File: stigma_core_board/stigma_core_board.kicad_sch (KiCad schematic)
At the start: 83 parts, among them J1 TC2050, J5 USB_C_Receptacle_USB2.0, SW1 KMR721NGLFS, SW2 KMR721NGLFS, U1 STM32H743VITx, U10 H3LIS331DL, U11 MS5607/MS5611, U12 LIS3MDL, U13 BMP580/BMP388/LPS22, U2 TPD4E1U06, U3 BMP580/BMP388/LPS22, U4 IIM-42652 (or other LGA-14 IM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, U5 AZ1117I-3.3, U6 ICM-42688 (or other LGA-14 IM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, U8 W25Q128JVP, U9 LSM6DSR, Y1 25MHz, Y2 32.768kHz

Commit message: First pass of signal routing
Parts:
- added C39, C40: 100n, Capacitor_SMD:C_0402_1005Metric, symbol Device:C_Small
- added R14: 4k7, Resistor_SMD:R_0402_1005Metric, symbol Device:R_Small
- added R15: 10k, Resistor_SMD:R_0402_1005Metric, symbol Device:R_Small
- added R16, R17, R18, R19, R20: 22, Resistor_SMD:R_0402_1005Metric, symbol Device:R_Small
- added U7: TPD4E1U06, Package_TO_SOT_SMD:SOT-563, symbol stigma:TPD4E001DRL
- J3: footprint stigma:DF40GB-70DP-0.4V -> stigma:DF40GB-70DP-0.4V-plug; symbol Connector_Generic:Conn_02x35_Top_Bottom -> Connector_Generic_Shielded:Conn_02x35_Top_Bottom_Shielded
- U2: footprint Package_TO_SOT_SMD:SOT-23-6 -> Package_TO_SOT_SMD:SOT-563; symbol Power_Protection:SRV05-4 -> stigma:TPD4E001DRL
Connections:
- net +3.3V: now also U7.5 (IO4)
- net +5V: now also C39.2, U7.6 (V_{cc})
- net BOOT: now also U2.2 (IO2), R20.1
- net D0+: now also U2.4 (IO3); no longer U2.6 (IO4)
- net D0-: now also U2.5 (IO4); no longer U2.4 (IO3)
- net GND: now also J3.SH (Shield), U2.3 (GND), C39.1, C40.1, R15.1, U7.3 (GND); no longer U2.2 (VN)
- net LED_GREEN: now also U1.77 (PA15)
- net LED_RED: now also U1.67 (PA8)
- net LED_YELLOW: now also U1.69 (PA10)
- net NRST: now also U2.1 (IO1), R17.1; no longer U1.14 (NRST)
- net SPI1_CS_BARO1: now also U1.83 (PD2)
- net SPI1_CS_HIGHG: now also U1.56 (PD9)
- net SPI1_CS_IMU1: now also U1.85 (PD4)
- net SPI1_CS_MAG: now also U1.86 (PD5)
- net SPI2_CS_BARO2: now also U1.3 (PE4)
- net SPI2_CS_BARO3: now also U1.2 (PE3)
- net SPI2_CS_IMU2: now also U1.55 (PD8)
- net SPI2_CS_IMU3: now also U1.7 (PC13)
- net SPI3_CS_FLASH: now also U1.87 (PD6); no longer U1.7 (PC13)
- net SWCLK: now also R16.2; no longer J1.6 (Pin_6)
- net SWDIO: now also R18.1; no longer J1.2 (Pin_2)
- net SWO: now also R19.1; no longer J1.5 (Pin_5)
- net USB_FS_VBUS: now also R14.1, R15.2
- net at D4.2 (A), J5.A4 (VBUS), J5.A9 (VBUS)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: now also U2.6 (V_{cc}), C40.2, R14.2; no longer U2.5 (VP)
- net BOOT0: no longer names the net of U1.94 (BOOT0)
- net BOOT0: now also R20.2
- net PA1 renamed PA1_ETH_REF_CLK
- net PA2 renamed PA2_ETH_MDIO
- net PA7 renamed PA7_ETH_CRS_DV
- net PB11 renamed PB11_ETH_TX_EN
- net PB12 renamed ETH_TXD-
- net PB13 renamed ETH_TXD+
- net PC1 renamed PC1_ETH_MDC
- net PC4 renamed ETH_RXD-
- net PC5 renamed ETH_RXD+
- new net: R17.2, U1.14 (NRST)
- new net: J1.5 (Pin_5), R19.2, U7.1 (IO1)
- new net: J1.2 (Pin_2), R18.2, U7.2 (IO2)
- new net: J1.6 (Pin_6), R16.1, U7.4 (IO3)
- no-connect marks 14 -> 18
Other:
- note added: "TODO: load cap values"
- note removed: "TODO: VBUS detection"
- note removed: "TODO: clamping diodes for buttons?"
- note removed: "TODO: place voltage dividers for battery voltage/current sensing here?"
- moved on the sheet: C15, C18, C19, C20, J1, R5, R6, SW1, SW2, U2, U5, U8

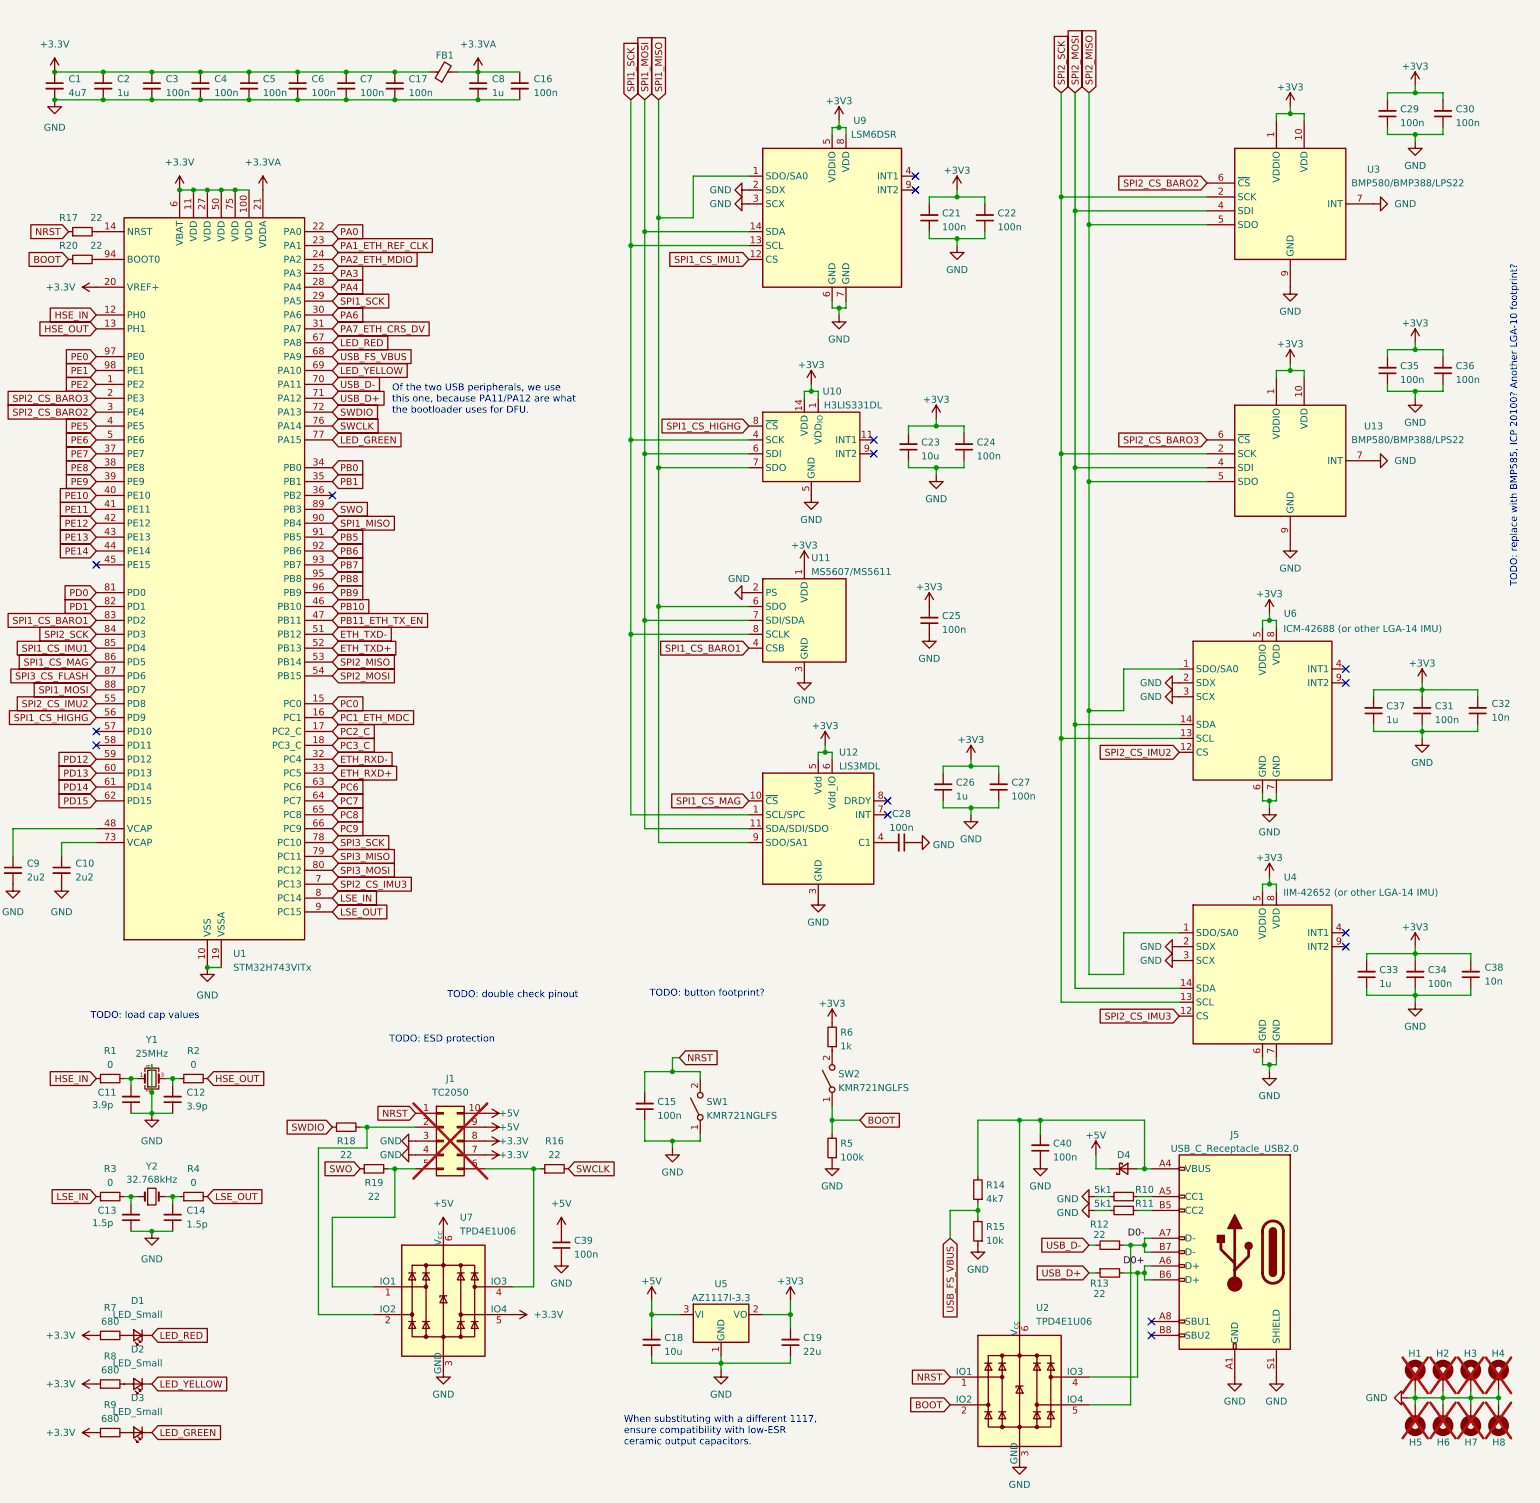
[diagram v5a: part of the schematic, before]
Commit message: Route power, please DRC
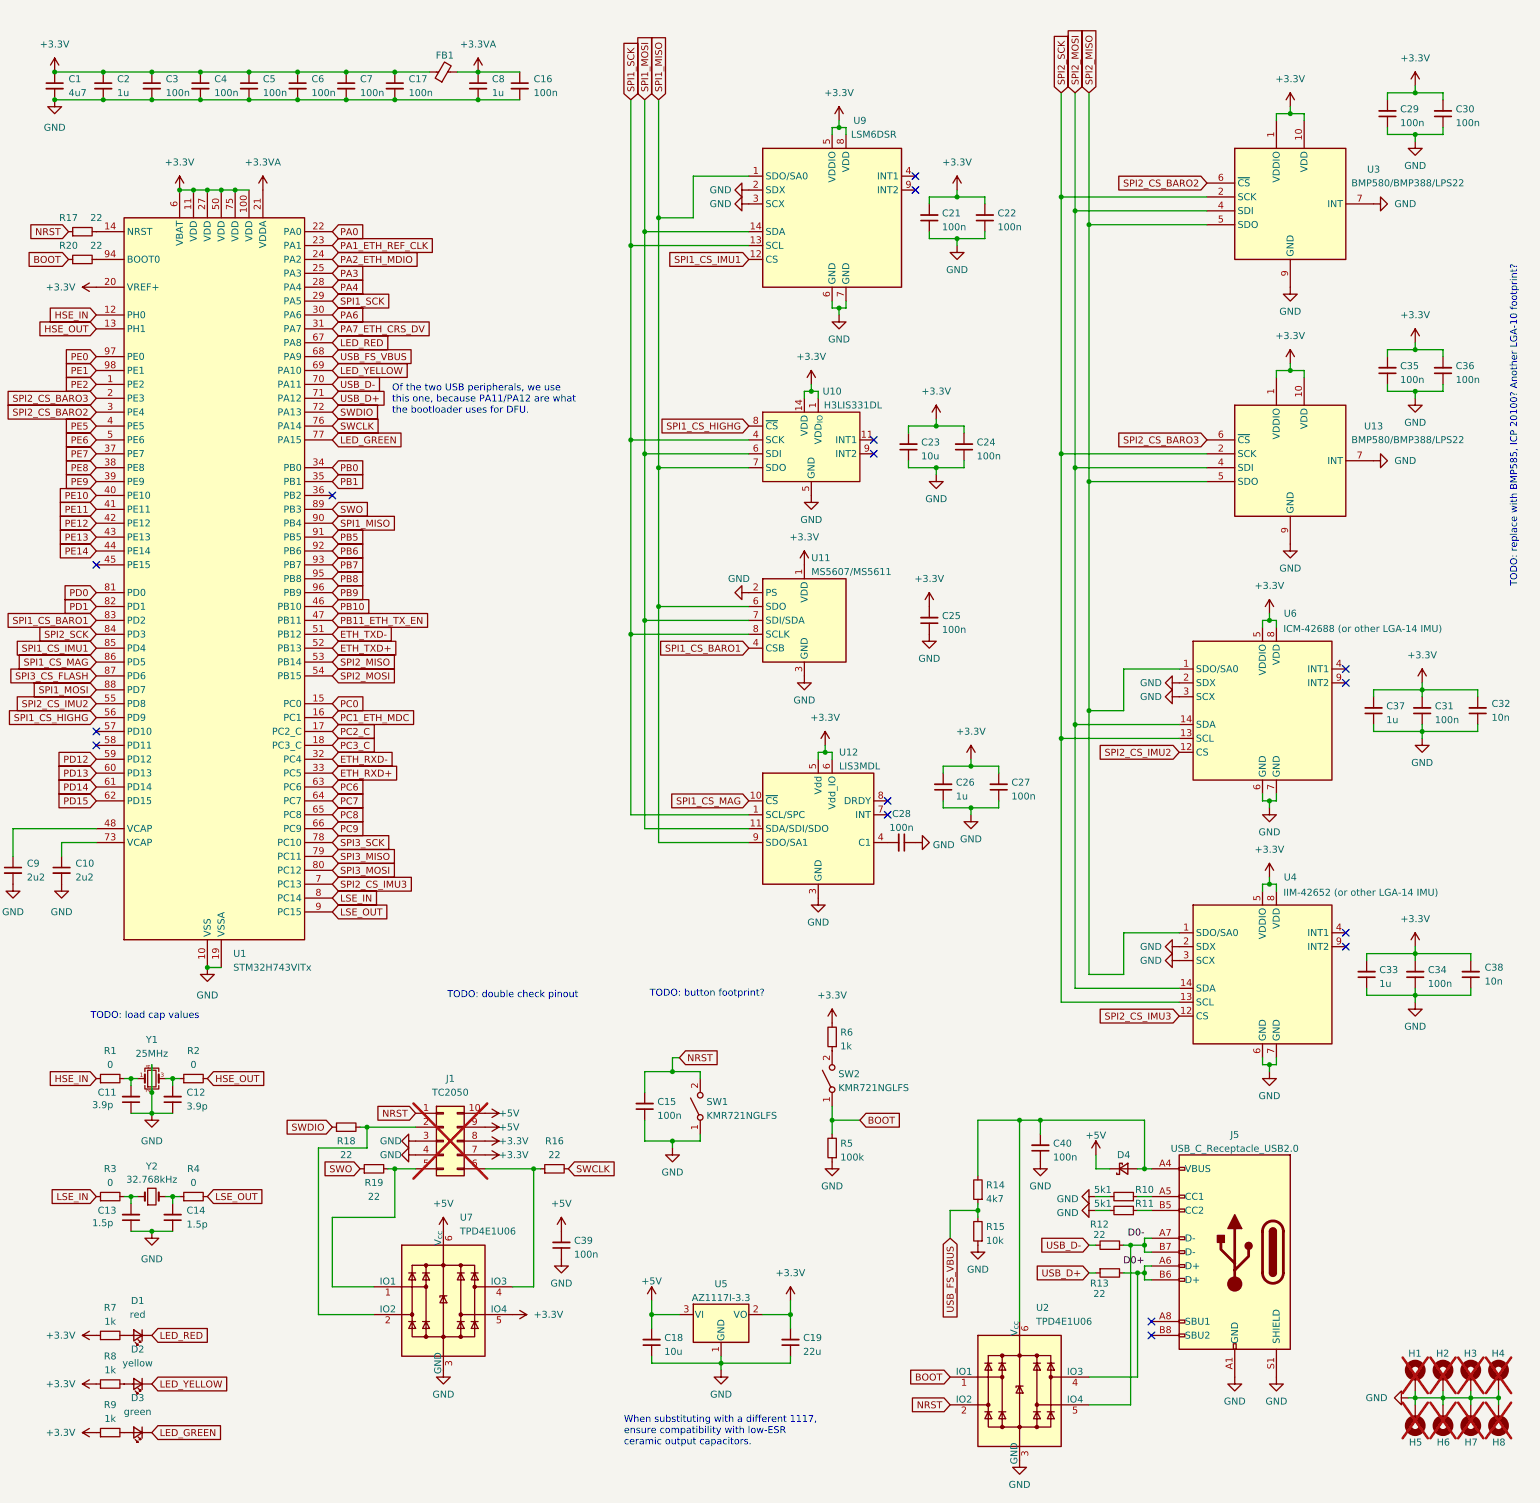
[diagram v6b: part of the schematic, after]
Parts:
- D1: value LED_Small -> red
- D2: value LED_Small -> yellow
- D3: value LED_Small -> green
- R7, R8, R9: value 680 -> 1k
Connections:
- net +3V3 is gone; now on net +3.3V: C19.2, C21.2, C22.2, C23.2, C24.2, C25.2, C26.2, C27.2, C29.2, C30.2, C31.2, C32.2, C33.2, C34.2, C35.2, C36.2, C37.2, C38.2, R6.2, U10.1 (VDD_{IO}), U10.14 (VDD), U10.15 (reserved), U11.1 (VDD), U12.5 (Vdd), U12.6 (Vdd_IO), U13.1 (VDDIO), U13.10 (VDD), U3.1 (VDDIO), U3.10 (VDD), U4.5 (VDDIO), U4.8 (VDD), U5.2 (VO), U6.5 (VDDIO), U6.8 (VDD), U9.5 (VDDIO), U9.8 (VDD)
- net BOOT: now also U2.1 (IO1); no longer U2.2 (IO2)
- net NRST: now also U2.2 (IO2); no longer U2.1 (IO1)
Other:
- note removed: "TODO: ESD protection"
